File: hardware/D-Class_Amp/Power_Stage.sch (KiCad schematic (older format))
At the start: 14 parts

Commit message: grounded man how it work
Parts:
- added D? (x2): D, symbol Device:D
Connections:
- net at U?.4 (DT): now also R?.2
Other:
- moved on the sheet: C?, Q?, R?, U?
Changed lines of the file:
@@
 L Driver_FET:IR21834 U?
 U 1 1 6104C522
-P 4200 2600
-F 0 "U?" H 4200 3281 50  0000 C CNN
-F 1 "IR21834" H 4200 3190 50  0000 C CNN
-F 2 "" H 4200 2600 50  0001 C CIN
-F 3 "https://www.infineon.com/dgdl/ir2183.pdf?fileId=5546d462533600a4015355c9490e16d1" H 4200 2600 50  0001 C CNN
-	1    4200 2600
+P 4200 2350
+F 0 "U?" H 4200 3031 50  0000 C CNN
+F 1 "IR21834" H 4200 2940 50  0000 C CNN
+F 2 "" H 4200 2350 50  0001 C CIN
+F 3 "https://www.infineon.com/dgdl/ir2183.pdf?fileId=5546d462533600a4015355c9490e16d1" H 4200 2350 50  0001 C CNN
+	1    4200 2350
 	1    0    0    -1
 $EndComp
@@
 L Device:Q_NMOS_GDSD Q?
 U 1 1 6104F024
-P 5400 2050
-F 0 "Q?" H 5688 2096 50  0000 L CNN
-F 1 "Q_NMOS_GDSD" H 5688 2005 50  0000 L CNN
-F 2 "" H 5600 2150 50  0001 C CNN
-F 3 "~" H 5400 2050 50  0001 C CNN
-	1    5400 2050
+P 5950 1950
+F 0 "Q?" H 6238 1996 50  0000 L CNN
+F 1 "Q_NMOS_GDSD" H 6238 1905 50  0000 L CNN
+F 2 "" H 6150 2050 50  0001 C CNN
+F 3 "~" H 5950 1950 50  0001 C CNN
+	1    5950 1950
 	1    0    0    -1
 $EndComp
@@
 L Device:Q_NMOS_GDSD Q?
 U 1 1 6104F394
-P 5450 3050
-F 0 "Q?" H 5738 3096 50  0000 L CNN
-F 1 "Q_NMOS_GDSD" H 5738 3005 50  0000 L CNN
-F 2 "" H 5650 3150 50  0001 C CNN
-F 3 "~" H 5450 3050 50  0001 C CNN
-	1    5450 3050
+P 5900 2750
+F 0 "Q?" H 6188 2796 50  0000 L CNN
+F 1 "Q_NMOS_GDSD" H 6188 2705 50  0000 L CNN
+F 2 "" H 6100 2850 50  0001 C CNN
+F 3 "~" H 5900 2750 50  0001 C CNN
+	1    5900 2750
 	1    0    0    -1
 $EndComp
@@
 L Device:R R?
 U 1 1 61051377
-P 5000 2400
-F 0 "R?" H 5070 2446 50  0000 L CNN
-F 1 "R" H 5070 2355 50  0000 L CNN
-F 2 "" V 4930 2400 50  0001 C CNN
-F 3 "~" H 5000 2400 50  0001 C CNN
-	1    5000 2400
-	1    0    0    -1
+P 5450 2000
+F 0 "R?" V 5243 2000 50  0000 C CNN
+F 1 "R" V 5334 2000 50  0000 C CNN
+F 2 "" V 5380 2000 50  0001 C CNN
+F 3 "~" H 5450 2000 50  0001 C CNN
+	1    5450 2000
+	0    1    1    0
 $EndComp
 $Comp
@@
 L Device:R R?
 U 1 1 61052B3F
-P 5000 4200
-F 0 "R?" H 5070 4246 50  0000 L CNN
-F 1 "R" H 5070 4155 50  0000 L CNN
-F 2 "" V 4930 4200 50  0001 C CNN
-F 3 "~" H 5000 4200 50  0001 C CNN
-	1    5000 4200
+P 5150 4350
+F 0 "R?" H 5220 4396 50  0000 L CNN
+F 1 "R" H 5220 4305 50  0000 L CNN
+F 2 "" V 5080 4350 50  0001 C CNN
+F 3 "~" H 5150 4350 50  0001 C CNN
+	1    5150 4350
 	1    0    0    -1
 $EndComp
@@
 L Device:R R?
 U 1 1 610540BF
-P 5050 3050
-F 0 "R?" H 5120 3096 50  0000 L CNN
-F 1 "R" H 5120 3005 50  0000 L CNN
-F 2 "" V 4980 3050 50  0001 C CNN
-F 3 "~" H 5050 3050 50  0001 C CNN
-	1    5050 3050
-	1    0    0    -1
+P 5400 2750
+F 0 "R?" V 5193 2750 50  0000 C CNN
+F 1 "R" V 5284 2750 50  0000 C CNN
+F 2 "" V 5330 2750 50  0001 C CNN
+F 3 "~" H 5400 2750 50  0001 C CNN
+	1    5400 2750
+	0    1    1    0
 $EndComp
 $Comp
 L Device:R R?
 U 1 1 61055141
-P 3700 2800
-F 0 "R?" V 3600 2800 50  0000 C CNN
-F 1 "R" V 3500 2800 50  0000 C CNN
-F 2 "" V 3630 2800 50  0001 C CNN
-F 3 "~" H 3700 2800 50  0001 C CNN
-	1    3700 2800
+P 3700 2550
+F 0 "R?" V 3600 2550 50  0000 C CNN
+F 1 "R" V 3500 2550 50  0000 C CNN
+F 2 "" V 3630 2550 50  0001 C CNN
+F 3 "~" H 3700 2550 50  0001 C CNN
+	1    3700 2550
 	0    -1   -1   0
 $EndComp
@@
 L power:VDD #PWR?
 U 1 1 6105D8A1
-P 2300 1600
-F 0 "#PWR?" H 2300 1450 50  0001 C CNN
-F 1 "VDD" H 2315 1773 50  0000 C CNN
-F 2 "" H 2300 1600 50  0001 C CNN
-F 3 "" H 2300 1600 50  0001 C CNN
-	1    2300 1600
+P 5950 1450
+F 0 "#PWR?" H 5950 1300 50  0001 C CNN
+F 1 "VDD" H 5965 1623 50  0000 C CNN
+F 2 "" H 5950 1450 50  0001 C CNN
+F 3 "" H 5950 1450 50  0001 C CNN
+	1    5950 1450
 	1    0    0    -1
 $EndComp
@@
 L power:GND #PWR?
 U 1 1 6105F7B4
-P 3400 1750
-F 0 "#PWR?" H 3400 1500 50  0001 C CNN
-F 1 "GND" H 3405 1577 50  0000 C CNN
-F 2 "" H 3400 1750 50  0001 C CNN
-F 3 "" H 3400 1750 50  0001 C CNN
-	1    3400 1750
+P 2800 3550
+F 0 "#PWR?" H 2800 3300 50  0001 C CNN
+F 1 "GND" H 2805 3377 50  0000 C CNN
+F 2 "" H 2800 3550 50  0001 C CNN
+F 3 "" H 2800 3550 50  0001 C CNN
+	1    2800 3550
 	1    0    0    -1
 $EndComp
@@
 L power:VSS #PWR?
 U 1 1 6105E48C
-P 2300 1800
-F 0 "#PWR?" H 2300 1650 50  0001 C CNN
-F 1 "VSS" H 2315 1973 50  0000 C CNN
-F 2 "" H 2300 1800 50  0001 C CNN
-F 3 "" H 2300 1800 50  0001 C CNN
-	1    2300 1800
+P 5950 3200
+F 0 "#PWR?" H 5950 3050 50  0001 C CNN
+F 1 "VSS" H 5965 3373 50  0000 C CNN
+F 2 "" H 5950 3200 50  0001 C CNN
+F 3 "" H 5950 3200 50  0001 C CNN
+	1    5950 3200
 	-1   0    0    1
 $EndComp
@@
 	1    0    0    -1
 $EndComp
-Text HLabel 3800 2600 0    50   Input ~ 0
+Text HLabel 3800 2350 0    50   Input ~ 0
 S-PWM
 Text HLabel 3650 4850 0    50   Input ~ 0
 ~S-PWM
-Text HLabel 6600 2550 0    50   Output ~ 0
+Text HLabel 6600 2300 0    50   Output ~ 0
 P_OUT
 Text HLabel 6650 4550 0    50   Output ~ 0
@@
 L Device:C_Small C?
 U 1 1 610A4CCB
-P 4750 1850
-F 0 "C?" H 4842 1896 50  0000 L CNN
-F 1 "C_Small" H 4842 1805 50  0000 L CNN
-F 2 "" H 4750 1850 50  0001 C CNN
-F 3 "~" H 4750 1850 50  0001 C CNN
-	1    4750 1850
+P 4700 1850
+F 0 "C?" H 4792 1896 50  0000 L CNN
+F 1 "C_Small" H 4792 1805 50  0000 L CNN
+F 2 "" H 4700 1850 50  0001 C CNN
+F 3 "~" H 4700 1850 50  0001 C CNN
+	1    4700 1850
 	1    0    0    -1
 $EndComp
@@
 L Device:C_Small C?
 U 1 1 610A52A3
-P 4700 4050
-F 0 "C?" H 4792 4096 50  0000 L CNN
-F 1 "C_Small" H 4792 4005 50  0000 L CNN
-F 2 "" H 4700 4050 50  0001 C CNN
-F 3 "~" H 4700 4050 50  0001 C CNN
-	1    4700 4050
+P 4800 4100
+F 0 "C?" H 4892 4146 50  0000 L CNN
+F 1 "C_Small" H 4892 4055 50  0000 L CNN
+F 2 "" H 4800 4100 50  0001 C CNN
+F 3 "~" H 4800 4100 50  0001 C CNN
+	1    4800 4100
 	1    0    0    -1
 $EndComp
@@
 L power:+12V #PWR?
 U 1 1 610ABD74
-P 3600 1550
-F 0 "#PWR?" H 3600 1400 50  0001 C CNN
-F 1 "+12V" H 3615 1723 50  0000 C CNN
-F 2 "" H 3600 1550 50  0001 C CNN
-F 3 "" H 3600 1550 50  0001 C CNN
-	1    3600 1550
-	1    0    0    -1
-$EndComp
-Wire Wire Line
-	3800 2600 3850 2600
-Wire Wire Line
-	3850 2600 3850 2700
-Wire Wire Line
-	3850 2700 3900 2700
-Connection ~ 3850 2600
-Wire Wire Line
-	3850 2600 3900 2600
+P 3100 2500
+F 0 "#PWR?" H 3100 2350 50  0001 C CNN
+F 1 "+12V" H 3115 2673 50  0000 C CNN
+F 2 "" H 3100 2500 50  0001 C CNN
+F 3 "" H 3100 2500 50  0001 C CNN
+	1    3100 2500
+	1    0    0    -1
+$EndComp
+Wire Wire Line
+	3800 2350 3850 2350
+Wire Wire Line
+	3850 2350 3850 2450
+Wire Wire Line
+	3850 2450 3900 2450
+Connection ~ 3850 2350
+Wire Wire Line
+	3850 2350 3900 2350
+$Comp
+L Device:D D?
+U 1 1 610CB2EC
+P 4400 1550
+F 0 "D?" H 4400 1333 50  0000 C CNN
+F 1 "D" H 4400 1424 50  0000 C CNN
+F 2 "" H 4400 1550 50  0001 C CNN
+F 3 "~" H 4400 1550 50  0001 C CNN
+	1    4400 1550
+	-1   0    0    1
+$EndComp
+$Comp
+L Device:D D?
+U 1 1 610CBA51
+P 4500 3750
+F 0 "D?" H 4500 3533 50  0000 C CNN
+F 1 "D" H 4500 3624 50  0000 C CNN
+F 2 "" H 4500 3750 50  0001 C CNN
+F 3 "~" H 4500 3750 50  0001 C CNN
+	1    4500 3750
+	-1   0    0    1
+$EndComp
+Wire Wire Line
+	3900 2550 3850 2550
+$Comp
+L power:VSS #PWR?
+U 1 1 610F7EDB
+P 5950 5600
+F 0 "#PWR?" H 5950 5450 50  0001 C CNN
+F 1 "VSS" H 5965 5773 50  0000 C CNN
+F 2 "" H 5950 5600 50  0001 C CNN
+F 3 "" H 5950 5600 50  0001 C CNN
+	1    5950 5600
+	-1   0    0    1
+$EndComp
+$Comp
+L power:VDD #PWR?
+U 1 1 610FA293
+P 6100 3800
+F 0 "#PWR?" H 6100 3650 50  0001 C CNN
+F 1 "VDD" H 6115 3973 50  0000 C CNN
+F 2 "" H 6100 3800 50  0001 C CNN
+F 3 "" H 6100 3800 50  0001 C CNN
+	1    6100 3800
+	1    0    0    -1
+$EndComp
 $EndSCHEMATC

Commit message: layout 1st pass
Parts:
- removed C?: C_Small, symbol Device:C_Small
- removed D?: D, symbol Device:D
- removed Q? (x2): Q_NMOS_GDSD, symbol Device:Q_NMOS_GDSD
- removed R? (x3): R, symbol Device:R
- removed U?: IR21834, symbol Driver_FET:IR21834
- added C?: C_Small, symbol Device:C_Small
- added D?: D, symbol Device:D
- added Q? (x2): Q_NMOS_GDSD, symbol Device:Q_NMOS_GDSD
- added R? (x3): R, symbol Device:R
- added U?: IR21834, symbol Driver_FET:IR21834
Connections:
- net +12V: now also D?.2 (A), U?.7 (VCC), D?.2 (A), U?.7 (VCC)
- net GND: now also R?.1, U?.3 (VSS), R?.1, U?.3 (VSS)
- net P_OUT: now also C?.2, Q?.2 (D), Q?.3 (S), Q?.4 (D), U?.11 (VS)
- net VDD: now also Q?.2 (D), Q?.4 (D), Q?.2 (D), Q?.4 (D)
- net VSS: now also Q?.3 (S), U?.5 (COM), Q?.3 (S), U?.5 (COM)
- net ~P_OUT: now also C?.2, Q?.2 (D), Q?.3 (S), Q?.4 (D), U?.11 (VS)
- net ~S-PWM: now also U?.1 (HIN), U?.2 (~LIN)
- net at U?.12 (HO): now also R?.2
- net at U?.13 (VB): now also C?.1, D?.1 (K)
- net at U?.6 (LO): now also R?.2
- net at Q?.1 (G): now also R?.1 (x2)
- new net: R?.2, U?.12 (HO)
- new net: C?.1, D?.1 (K), U?.13 (VB)
- new net: R?.2, U?.4 (DT)
- new net: R?.2, U?.6 (LO)
- new net: Q?.1 (G), R?.1 (x2)
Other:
- moved on the sheet: C?, D?, Q?, R?, U?

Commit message: anot
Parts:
- Q301, Q302, Q303, Q304: renamed from Q?; value Q_NMOS_GDSD -> PHP23NQ11T
- gave numbers to parts that had none: 12
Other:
- note added: "Inverting Half-Bridge\n"
- note added: "Non-Inverting Half-Bridge\n"
- moved on the sheet: C1, C2, D1, D2, Q301, Q302, Q303, Q304, R301, R302, R303, R304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

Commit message: single side
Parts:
- added C303 (x2): 10u, symbol Device:C_Small
- added U303: NCP1117-12_TO252, Package_TO_SOT_SMD:TO-252-2, symbol Regulator_Linear:NCP1117-12_TO252
- R301, R302, R303, R304, R305, R306: value R -> 10
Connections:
- net VSS is gone; now on net GND: Q302.3 (S), Q304.3 (S), U301.5 (COM), U302.5 (COM)
- net +12V: now also C303.1, U303.2 (VO)
- net GND: now also C303.2, C303.2, U303.1 (GND)
- net VDD: now also C303.1, U303.3 (VI)
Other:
- note added: "12V Reg\n\n"
- moved on the sheet: C1, C2, D1, D2, Q301, Q302, Q303, Q304, R301, R302, R303, R304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

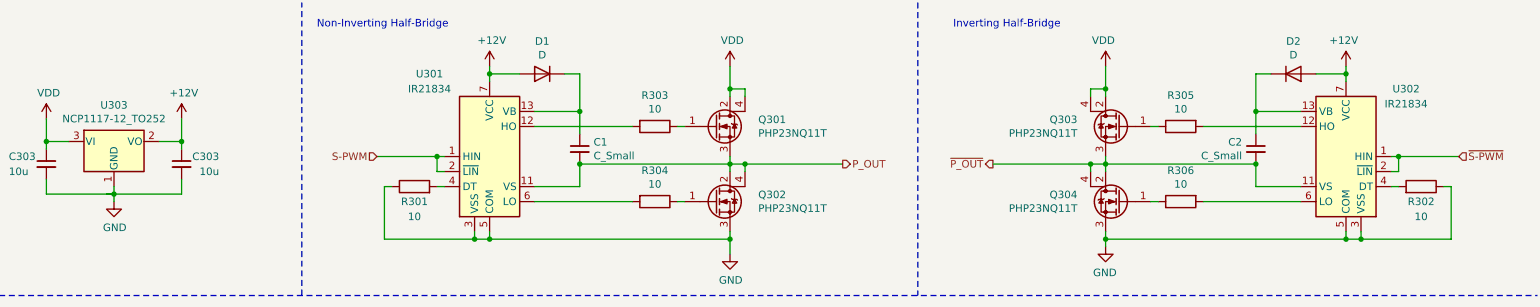
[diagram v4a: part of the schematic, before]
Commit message: deat time and values, 12v reg
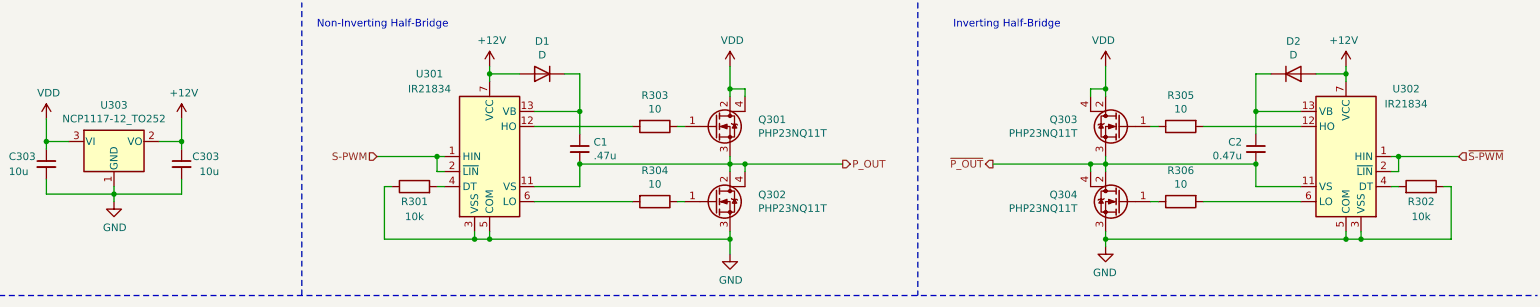
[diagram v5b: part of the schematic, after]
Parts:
- C1: value C_Small -> .47u
- C2: value C_Small -> 0.47u
- R301, R302: value 10 -> 10k
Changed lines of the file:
@@
 P 4850 1450
 F 0 "C1" H 4942 1496 50  0000 L CNN
-F 1 "C_Small" H 4942 1405 50  0000 L CNN
+F 1 ".47u" H 4942 1405 50  0000 L CNN
 F 2 "" H 4850 1450 50  0001 C CNN
 F 3 "~" H 4850 1450 50  0001 C CNN
@@
 P 3750 1700
 F 0 "R301" V 3650 1700 50  0000 C CNN
-F 1 "10" V 3550 1700 50  0000 C CNN
+F 1 "10k" V 3550 1700 50  0000 C CNN
 F 2 "" V 3680 1700 50  0001 C CNN
 F 3 "~" H 3750 1700 50  0001 C CNN
@@
 P 9350 1450
 F 0 "C2" H 9442 1496 50  0000 L CNN
-F 1 "C_Small" H 9442 1405 50  0000 L CNN
+F 1 "0.47u" H 9442 1405 50  0000 L CNN
 F 2 "" H 9350 1450 50  0001 C CNN
 F 3 "~" H 9350 1450 50  0001 C CNN
@@
 P 10450 1700
 F 0 "R302" V 10350 1700 50  0000 C CNN
-F 1 "10" V 10250 1700 50  0000 C CNN
+F 1 "10k" V 10250 1700 50  0000 C CNN
 F 2 "" V 10380 1700 50  0001 C CNN
 F 3 "~" H 10450 1700 50  0001 C CNN
@@
 12V Reg\n\n
 Wire Wire Line
-	1700 1750 1750 1750
-Wire Wire Line
 	1300 1750 1750 1750

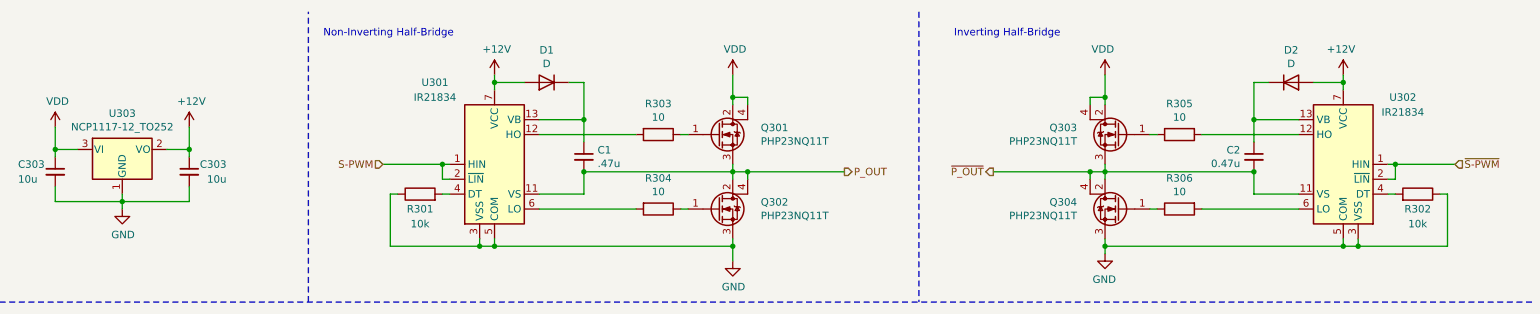
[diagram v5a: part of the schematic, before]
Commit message: Added input bias circuit and gain stage to input-stage schematic.
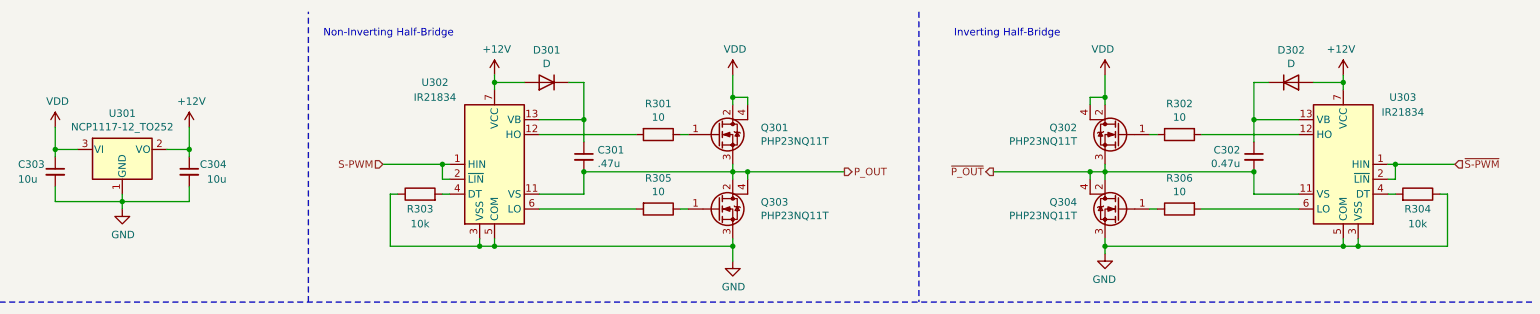
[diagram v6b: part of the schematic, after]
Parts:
- renumbered C1 to C301, C2 to C302, C303 to C304, D1 to D301, D2 to D302, Q303 to Q302, Q302 to Q303, R303 to R301, R305 to R302, R301 to R303, R302 to R304, R304 to R305, U303 to U301, U301 to U302, U302 to U303
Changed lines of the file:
@@
 $EndDescr
 $Comp
-L power:VDD #PWR0109
+L power:VDD #PWR0302
 U 1 1 6105D8A1
 P 5850 900
-F 0 "#PWR0109" H 5850 750 50  0001 C CNN
+F 0 "#PWR0302" H 5850 750 50  0001 C CNN
 F 1 "VDD" H 5865 1073 50  0000 C CNN
 F 2 "" H 5850 900 50  0001 C CNN
@@
 S-PWM
 $Comp
-L Device:C_Small C1
+L Device:C_Small C301
 U 1 1 610A4CCB
 P 4850 1450
-F 0 "C1" H 4942 1496 50  0000 L CNN
+F 0 "C301" H 4942 1496 50  0000 L CNN
 F 1 ".47u" H 4942 1405 50  0000 L CNN
 F 2 "" H 4850 1450 50  0001 C CNN
@@
 $EndComp
 $Comp
-L power:+12V #PWR0112
+L power:+12V #PWR0301
 U 1 1 610ABD74
 P 4250 900
-F 0 "#PWR0112" H 4250 750 50  0001 C CNN
+F 0 "#PWR0301" H 4250 750 50  0001 C CNN
 F 1 "+12V" H 4265 1073 50  0000 C CNN
 F 2 "" H 4250 900 50  0001 C CNN
@@
 	3900 1500 3950 1500
 $Comp
-L Device:D D1
+L Device:D D301
 U 1 1 610CB2EC
 P 4600 950
-F 0 "D1" H 4600 733 50  0000 C CNN
+F 0 "D301" H 4600 733 50  0000 C CNN
 F 1 "D" H 4600 824 50  0000 C CNN
 F 2 "" H 4600 950 50  0001 C CNN
@@
 Non-Inverting Half-Bridge\n
 $Comp
-L Device:R R304
+L Device:R R305
 U 1 1 610540BF
 P 5350 1800
-F 0 "R304" V 5143 1800 50  0000 C CNN
+F 0 "R305" V 5143 1800 50  0000 C CNN
 F 1 "10" V 5234 1800 50  0000 C CNN
 F 2 "" V 5280 1800 50  0001 C CNN
@@
 $EndComp
 $Comp
-L Device:R R303
+L Device:R R301
 U 1 1 61051377
 P 5350 1300
-F 0 "R303" V 5143 1300 50  0000 C CNN
+F 0 "R301" V 5143 1300 50  0000 C CNN
 F 1 "10" V 5234 1300 50  0000 C CNN
 F 2 "" V 5280 1300 50  0001 C CNN
@@
 $EndComp
 $Comp
-L Device:R R301
+L Device:R R303
 U 1 1 61055141
 P 3750 1700
-F 0 "R301" V 3650 1700 50  0000 C CNN
+F 0 "R303" V 3650 1700 50  0000 C CNN
 F 1 "10k" V 3550 1700 50  0000 C CNN
 F 2 "" V 3680 1700 50  0001 C CNN
@@
 $EndComp
 $Comp
-L Device:Q_NMOS_GDSD Q302
+L Device:Q_NMOS_GDSD Q303
 U 1 1 6104F394
 P 5750 1800
-F 0 "Q302" H 6038 1846 50  0000 L CNN
+F 0 "Q303" H 6038 1846 50  0000 L CNN
 F 1 "PHP23NQ11T" H 6038 1755 50  0000 L CNN
 F 2 "" H 5950 1900 50  0001 C CNN
@@
 $EndComp
 $Comp
-L Driver_FET:IR21834 U301
+L Driver_FET:IR21834 U302
 U 1 1 6104C522
 P 4250 1500
-F 0 "U301" H 3850 2050 50  0000 C CNN
+F 0 "U302" H 3850 2050 50  0000 C CNN
 F 1 "IR21834" H 3850 1950 50  0000 C CNN
 F 2 "" H 4250 1500 50  0001 C CIN
@@
 $EndComp
 $Comp
-L power:GND #PWR?
+L power:GND #PWR0309
 U 1 1 6107E9DB
 P 5850 2150
-F 0 "#PWR?" H 5850 1900 50  0001 C CNN
+F 0 "#PWR0309" H 5850 1900 50  0001 C CNN
 F 1 "GND" H 5855 1977 50  0000 C CNN
 F 2 "" H 5850 2150 50  0001 C CNN
@@
 	5850 2050 5850 2150
 $Comp
-L power:GND #PWR?
+L power:GND #PWR0308
 U 1 1 610A1CEE
 P 8350 2100
-F 0 "#PWR?" H 8350 1850 50  0001 C CNN
+F 0 "#PWR0308" H 8350 1850 50  0001 C CNN
 F 1 "GND" H 8355 1927 50  0000 C CNN
 F 2 "" H 8350 2100 50  0001 C CNN
@@
 $EndComp
 $Comp
-L Device:Q_NMOS_GDSD Q303
+L Device:Q_NMOS_GDSD Q302
 U 1 1 610F221C
 P 8450 1300
-F 0 "Q303" H 8738 1346 50  0000 L CNN
+F 0 "Q302" H 8738 1346 50  0000 L CNN
 F 1 "PHP23NQ11T" H 8738 1255 50  0000 L CNN
 F 2 "" H 8650 1400 50  0001 C CNN
@@
 $EndComp
 $Comp
-L Driver_FET:IR21834 U302
+L Driver_FET:IR21834 U303
 U 1 1 610F2212
 P 9950 1500
-F 0 "U302" H 9550 1950 50  0000 C CNN
+F 0 "U303" H 9550 1950 50  0000 C CNN
 F 1 "IR21834" H 9550 1850 50  0000 C CNN
 F 2 "" H 9950 1500 50  0001 C CIN
@@
 $EndComp
 $Comp
-L Device:R R305
+L Device:R R302
 U 1 1 610F2230
 P 8850 1300
-F 0 "R305" V 8643 1300 50  0000 C CNN
+F 0 "R302" V 8643 1300 50  0000 C CNN
 F 1 "10" V 8734 1300 50  0000 C CNN
 F 2 "" V 8780 1300 50  0001 C CNN
@@
 	10250 1700 10300 1700
 $Comp
-L Device:D D2
+L Device:D D302
 U 1 1 610F2287
 P 9600 950
-F 0 "D2" H 9600 733 50  0000 C CNN
+F 0 "D302" H 9600 733 50  0000 C CNN
 F 1 "D" H 9600 824 50  0000 C CNN
 F 2 "" H 9600 950 50  0001 C CNN
@@
 	10700 1500 10300 1500
 $Comp
-L power:+12V #PWR0116
+L power:+12V #PWR0304
 U 1 1 610F2278
 P 9950 900
-F 0 "#PWR0116" H 9950 750 50  0001 C CNN
+F 0 "#PWR0304" H 9950 750 50  0001 C CNN
 F 1 "+12V" H 9965 1073 50  0000 C CNN
 F 2 "" H 9950 900 50  0001 C CNN
@@
 $EndComp
 $Comp
-L Device:C_Small C2
+L Device:C_Small C302
 U 1 1 610F226E
 P 9350 1450
-F 0 "C2" H 9442 1496 50  0000 L CNN
+F 0 "C302" H 9442 1496 50  0000 L CNN
 F 1 "0.47u" H 9442 1405 50  0000 L CNN
 F 2 "" H 9350 1450 50  0001 C CNN
@@
 $EndComp
 $Comp
-L power:VDD #PWR0113
+L power:VDD #PWR0303
 U 1 1 610F224E
 P 8350 900
-F 0 "#PWR0113" H 8350 750 50  0001 C CNN
+F 0 "#PWR0303" H 8350 750 50  0001 C CNN
 F 1 "VDD" H 8365 1073 50  0000 C CNN
 F 2 "" H 8350 900 50  0001 C CNN
@@
 $EndComp
 $Comp
-L Device:R R302
+L Device:R R304
 U 1 1 610F2244
 P 10450 1700
-F 0 "R302" V 10350 1700 50  0000 C CNN
+F 0 "R304" V 10350 1700 50  0000 C CNN
 F 1 "10k" V 10250 1700 50  0000 C CNN
 F 2 "" V 10380 1700 50  0001 C CNN
@@
 	3550 2050 4150 2050
 $Comp
-L Regulator_Linear:NCP1117-12_TO252 U303
+L Regulator_Linear:NCP1117-12_TO252 U301
 U 1 1 61102BEC
 P 1750 1400
-F 0 "U303" H 1750 1642 50  0000 C CNN
+F 0 "U301" H 1750 1642 50  0000 C CNN
 F 1 "NCP1117-12_TO252" H 1750 1551 50  0000 C CNN
 F 2 "Package_TO_SOT_SMD:TO-252-2" H 1750 1625 50  0001 C CNN
@@
 $EndComp
 $Comp
-L power:+12V #PWR?
+L power:+12V #PWR0306
 U 1 1 61106009
 P 2200 1250
-F 0 "#PWR?" H 2200 1100 50  0001 C CNN
+F 0 "#PWR0306" H 2200 1100 50  0001 C CNN
 F 1 "+12V" H 2215 1423 50  0000 C CNN
 F 2 "" H 2200 1250 50  0001 C CNN
@@
 $EndComp
 $Comp
-L power:VDD #PWR?
+L power:VDD #PWR0305
 U 1 1 61109C5A
 P 1300 1250
-F 0 "#PWR?" H 1300 1100 50  0001 C CNN
+F 0 "#PWR0305" H 1300 1100 50  0001 C CNN
 F 1 "VDD" H 1315 1423 50  0000 C CNN
 F 2 "" H 1300 1250 50  0001 C CNN
@@
 $EndComp
 $Comp
-L power:GND #PWR?
+L power:GND #PWR0307
 U 1 1 6110DE87
 P 1750 1800
-F 0 "#PWR?" H 1750 1550 50  0001 C CNN
+F 0 "#PWR0307" H 1750 1550 50  0001 C CNN
 F 1 "GND" H 1755 1627 50  0000 C CNN
 F 2 "" H 1750 1800 50  0001 C CNN
@@
 $EndComp
 $Comp
-L Device:C_Small C303
+L Device:C_Small C304
 U 1 1 6116D137
 P 2200 1550
-F 0 "C303" H 1950 1600 50  0000 L CNN
+F 0 "C304" H 1950 1600 50  0000 L CNN
 F 1 "10u" H 1950 1500 50  0000 L CNN
 F 2 "" H 2200 1550 50  0001 C CNN
